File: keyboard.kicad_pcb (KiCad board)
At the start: 2 copper layers, 203.4 x 107.7 mm, 50 parts, among them J1 TRRS, SW00 Key, SW01 Key, SW02 Key, SW03 Key, SW10 Key, SW11 Key, SW12 Key, SW13 Key, SW14 Key, SW15 Key, SW16 Key, SW17 Key, SW18 Key, SW20 Key, SW21 Key, SW22 Key, SW23 Key, SW24 Key, SW25 Key, SW26 Key, SW27 Key, SW28 Key, SW30 Key, SW31 Key, SW32 Key, SW33 Key, SW34 Key, SW35 Key, SW36 Key, SW37 Key, SW38 Key, SW40 Key, SW41 Key, SW42 Key, SW43 Key, SW44 Key, SW45 Key, SW46 Key, SW47 Key, SW48 Key, U1 ProMicro

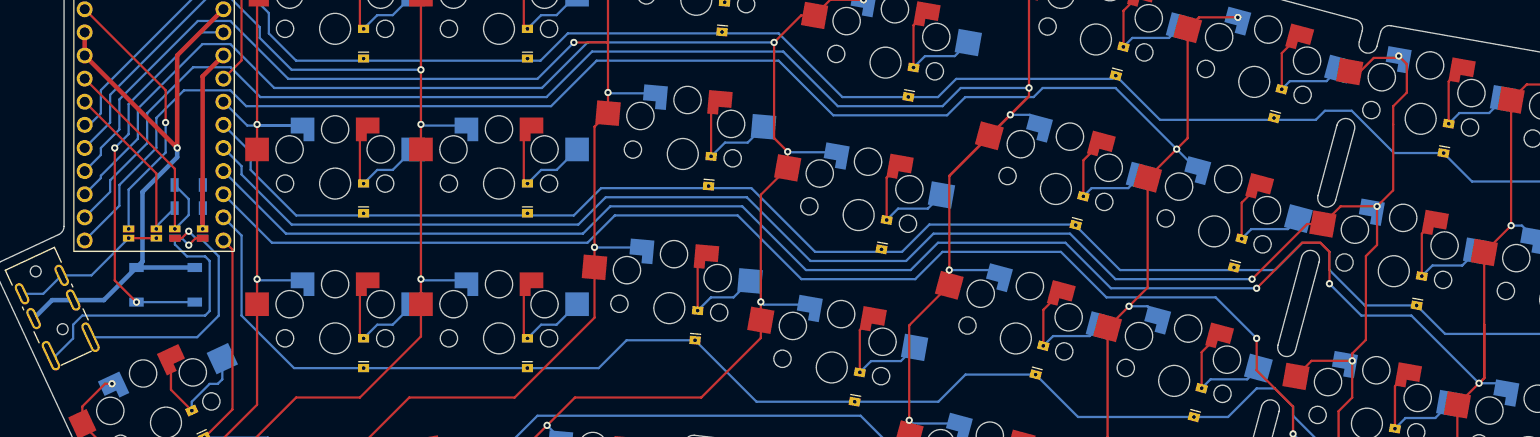
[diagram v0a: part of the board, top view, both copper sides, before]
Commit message: fix more traces
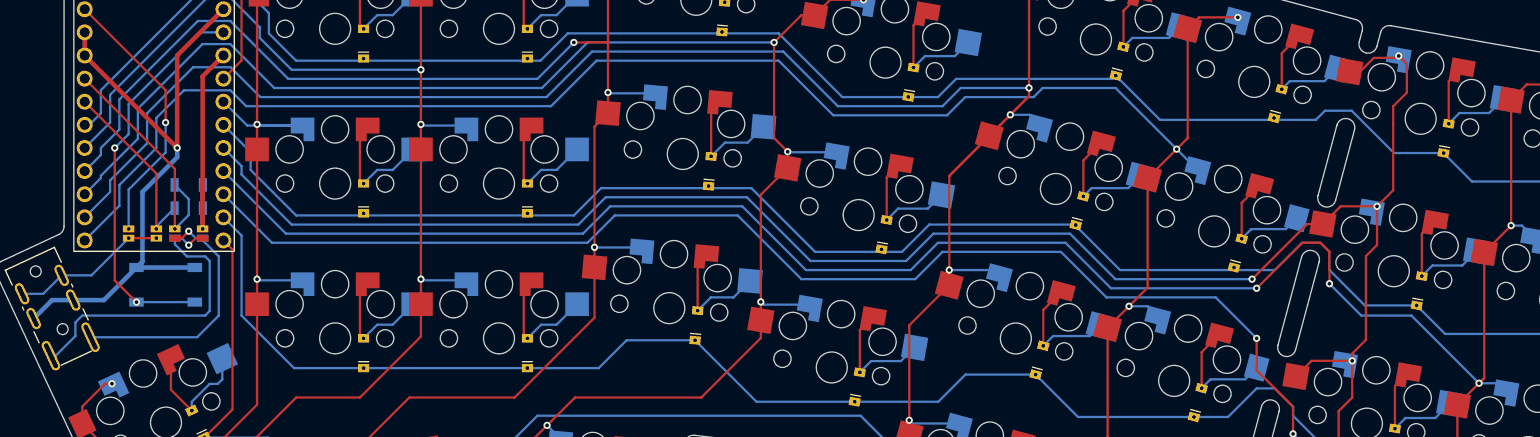
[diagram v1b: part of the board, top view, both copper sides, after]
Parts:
- SW15, SW25, SW35: footprint keyboard:Key -> keyboard:KeyRight
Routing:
- net col7: track 241.1 -> 235.3 mm

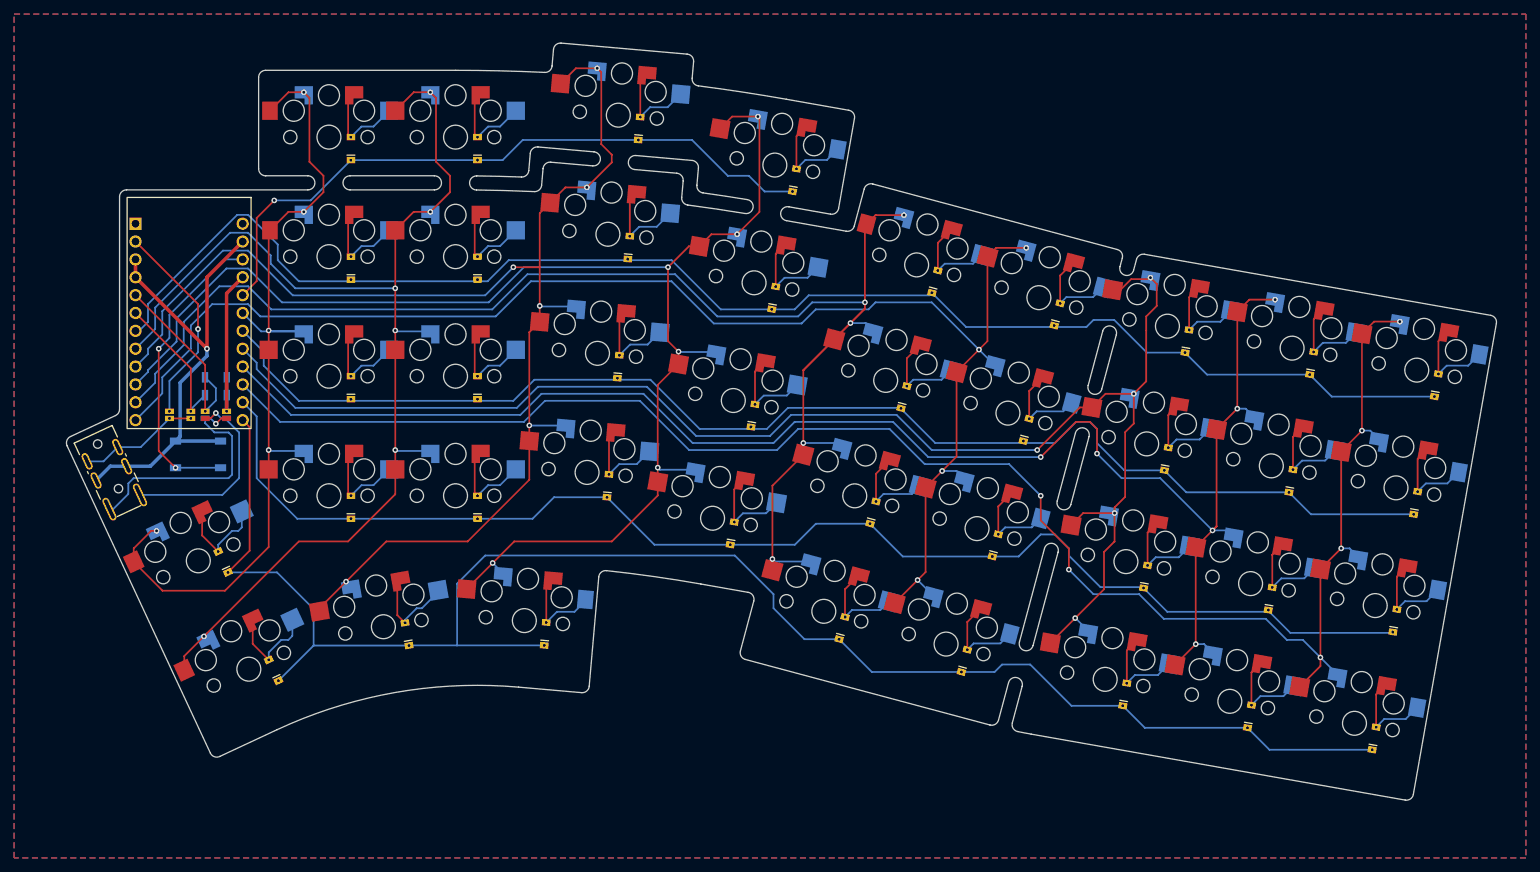
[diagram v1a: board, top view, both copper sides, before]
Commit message: improve more traces
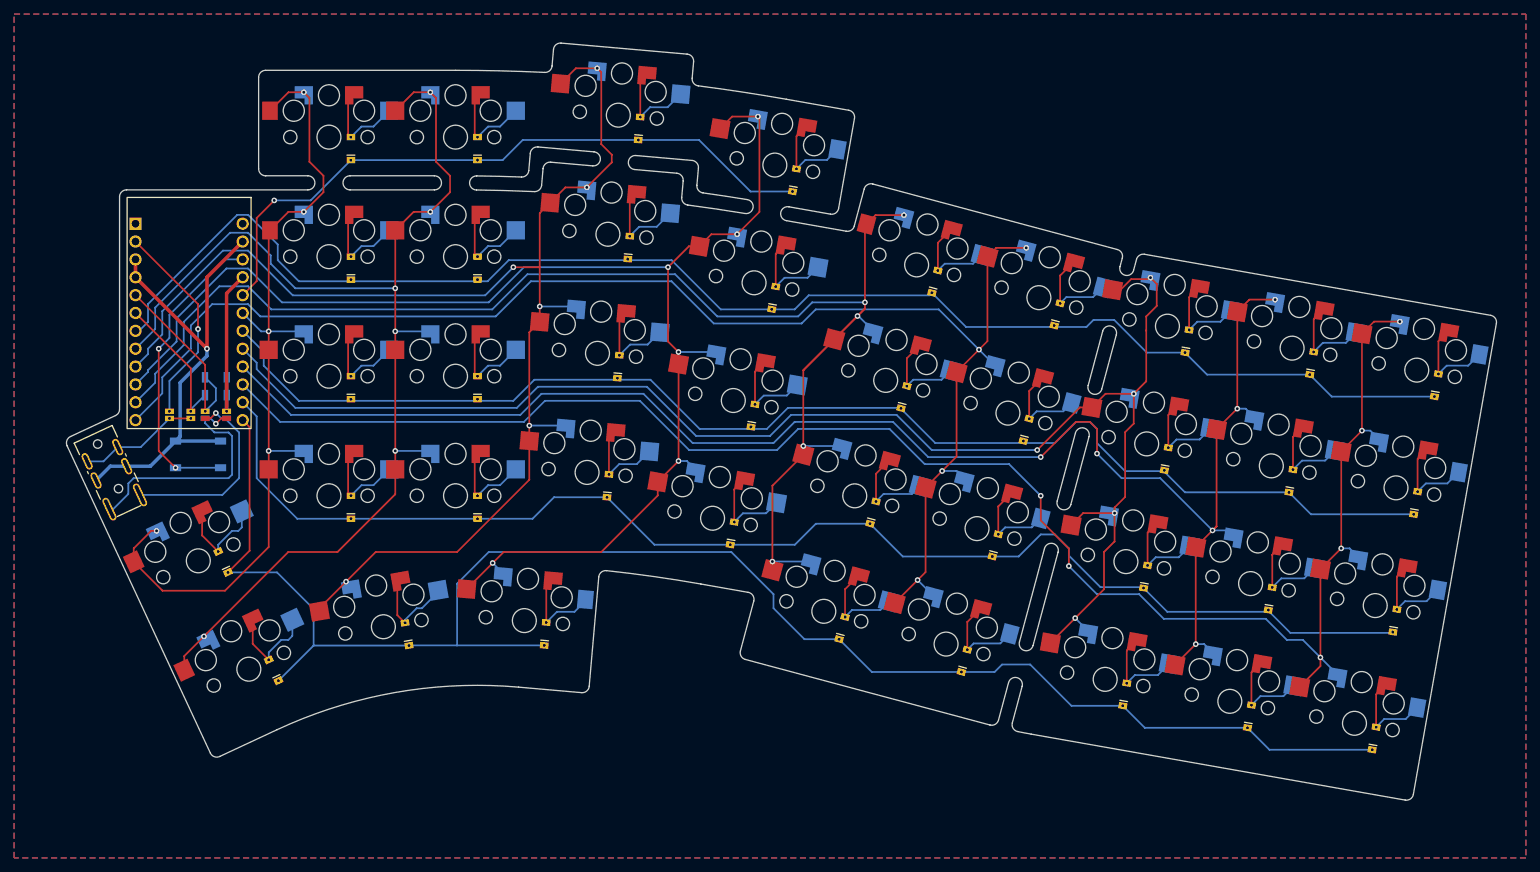
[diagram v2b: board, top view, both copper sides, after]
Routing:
- net col0: track 125.8 -> 120.7 mm
- net col3: track 211.4 -> 208.8 mm
- net col4: track 208.0 -> 207.1 mm
- net col5: track 209.9 -> 209.1 mm
